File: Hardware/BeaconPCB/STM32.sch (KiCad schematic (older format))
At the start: 22 parts, among them U2 STM32F042C6T6

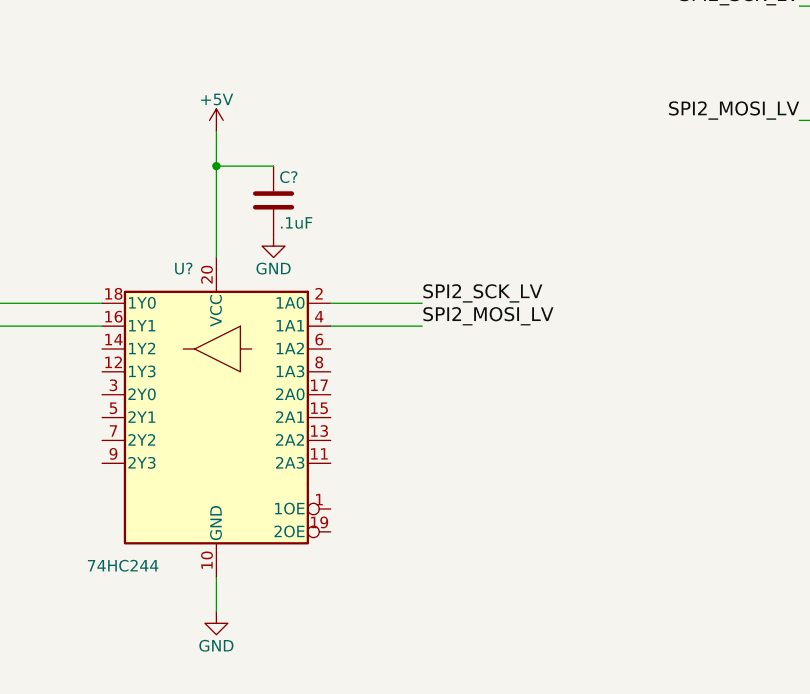
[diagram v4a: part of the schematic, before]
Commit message: SPi buffer schematic update.
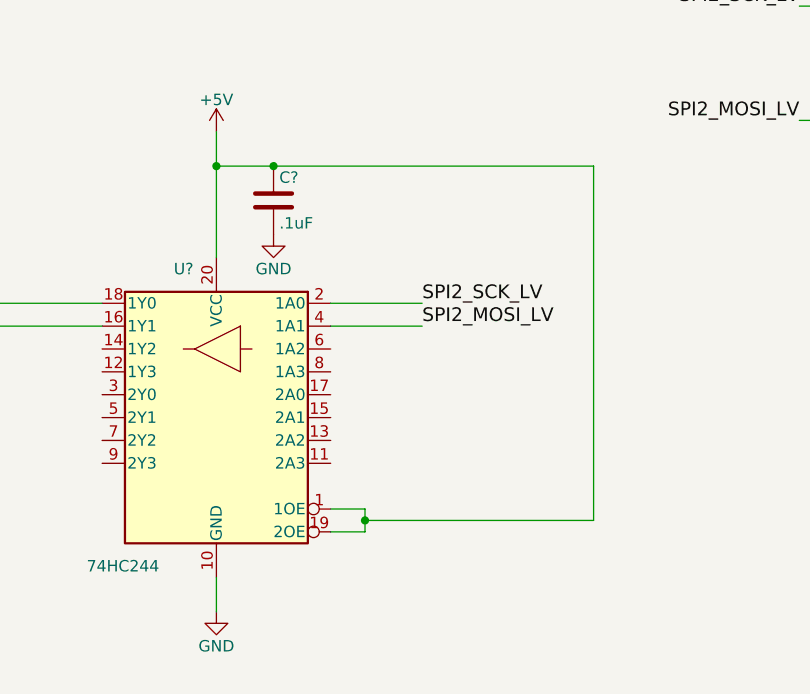
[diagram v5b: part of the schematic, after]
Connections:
- net +5V: now also U?.1 (1OE), U?.19 (2OE)
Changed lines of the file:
@@
 LIBS:contrib
 LIBS:valves
-LIBS:STM32F042C6T6
-LIBS:crumpschemes
 LIBS:Hex-Beacons-cache
 EELAYER 25 0
@@
 	3050 5850 3050 6400
 Wire Wire Line
-	3300 6000 3050 6000
+	3050 6000 4700 6000
 Wire Wire Line
 	3550 6700 3950 6700
@@
 Wire Wire Line
 	6400 3000 5550 3000
+Wire Wire Line
+	3550 7500 3700 7500
+Wire Wire Line
+	3700 7500 3700 7600
+Wire Wire Line
+	3700 7600 3550 7600
+Wire Wire Line
+	3700 7550 4700 7550
+Wire Wire Line
+	4700 7550 4700 6000
+Connection ~ 3300 6000
+Connection ~ 3700 7550
 $EndSCHEMATC
